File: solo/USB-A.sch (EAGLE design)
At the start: 27 parts, among them U1 USB_TRACES

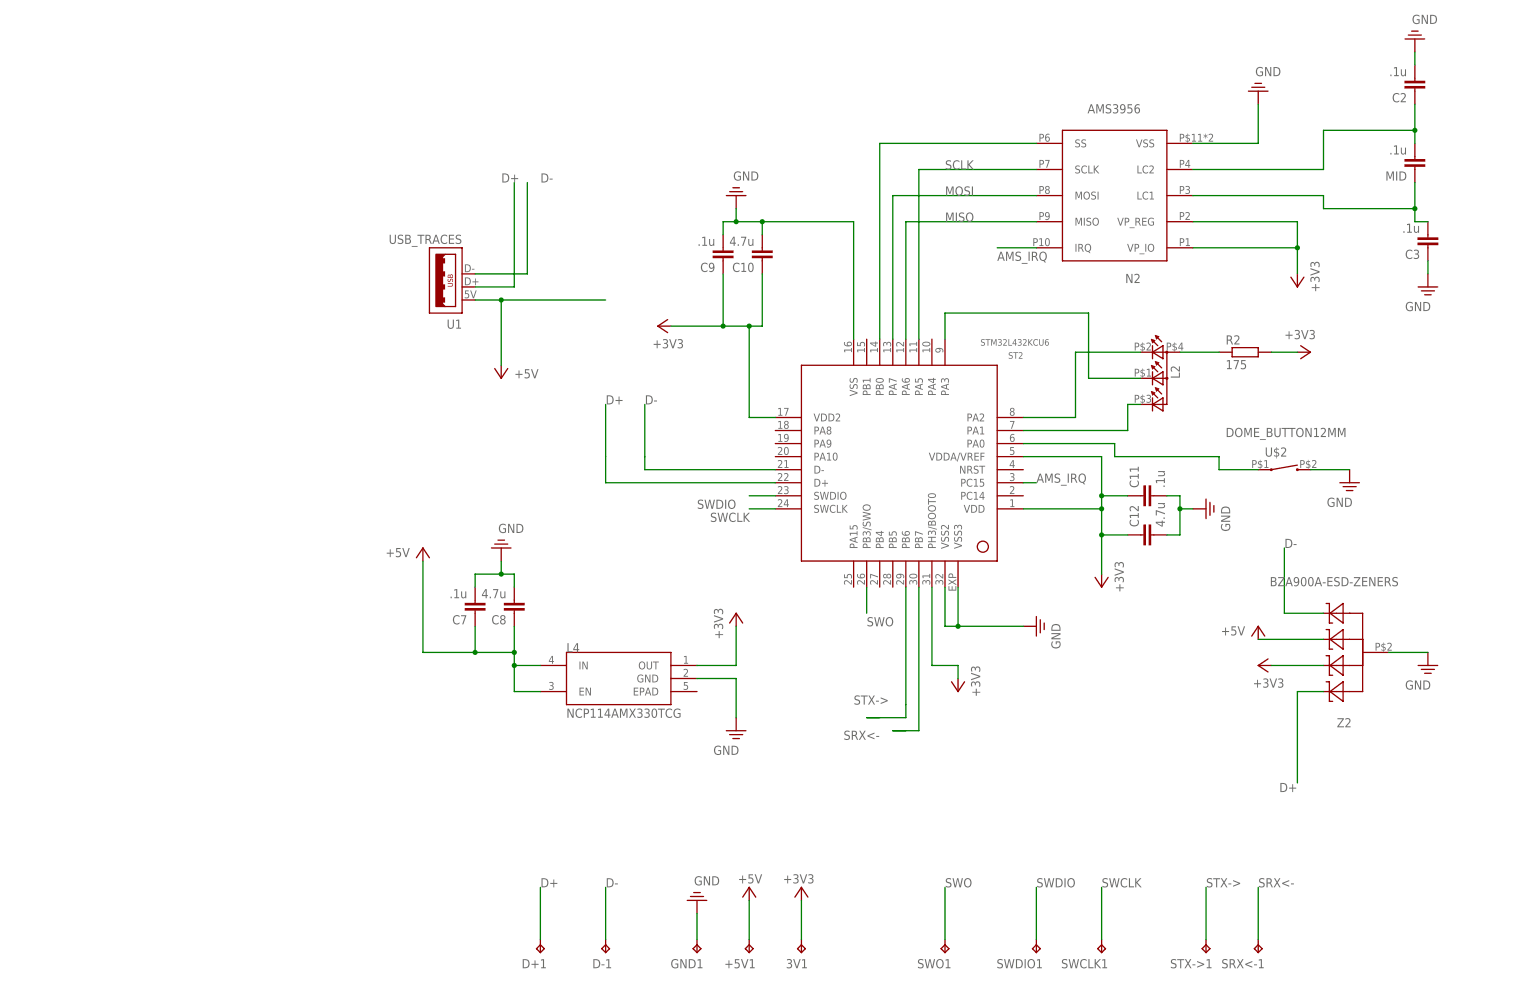
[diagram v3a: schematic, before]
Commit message: NFC designs
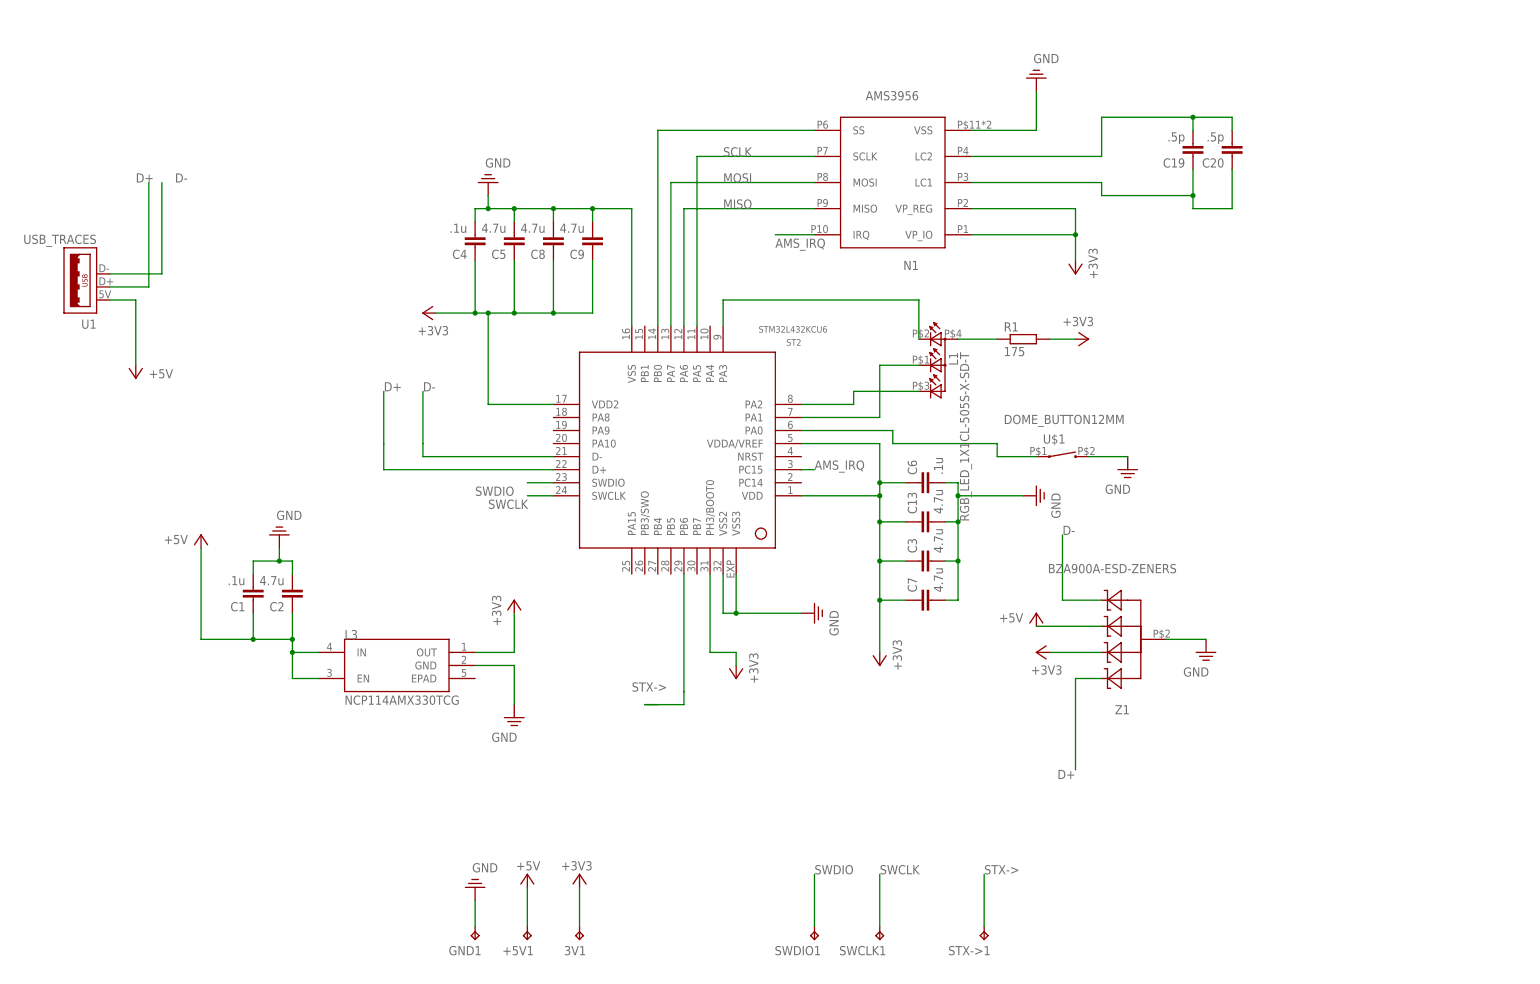
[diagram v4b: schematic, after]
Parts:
- removed C10, C12: 4.7u, efm-fido:CAPACITOR
- removed C11, MID: .1u, efm-fido:CAPACITOR
- removed D+1, D-1, SRX<-1, SWO1: TEST_POINT, efm-fido:TEST_POINT
- removed L2: EAST1616RGBA3-LED-RGBCL-505S-X-SD-T, efm-fido:EAST1616RGBA3-LED-RGBCL-505S-X-SD-T
- removed L4: NCP114AMX330TCG, efm-fido:NCP114AMX330TCG
- removed N2: AMS3956, efm-fido:AMS3956
- removed R2: 175, efm-fido:RESISTOR
- removed U$2: DOME_BUTTON12MM, efm-fido:DOME_BUTTON12MM
- removed Z2: BZA900A-ESD-ZENERS, efm-fido:BZA900A-ESD-ZENERS
- added C1, C4, C6: .1u, efm-fido:CAPACITOR
- added C13, C5: 4.7u, efm-fido:CAPACITOR
- added C19, C20: .5p, efm-fido:CAPACITOR
- added L1: RGB_LED_1X1CL-505S-X-SD-T, efm-fido:RGB_LED_1X1CL-505S-X-SD-T
- added L3: NCP114AMX330TCG, efm-fido:NCP114AMX330TCG
- added N1: AMS3956, efm-fido:AMS3956
- added R1: 175, efm-fido:RESISTOR
- added U$1: DOME_BUTTON12MM, efm-fido:DOME_BUTTON12MM
- added Z1: BZA900A-ESD-ZENERS, efm-fido:BZA900A-ESD-ZENERS
- C2, C3, C7, C9: value .1u -> 4.7u
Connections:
- removed net AMS_CS: N2.SS, ST2.PB0
- removed net N$18: L2.CGREEN, ST2.PA1
- removed net N$19: ST2.PA0, U$2.1
- removed net N$25: C2.1, MID.2, N2.LC2
- removed net N$26: C3.2, MID.1, N2.LC1
- removed net SRX<-: SRX<-1.TP, ST2.PB7
- removed net SWO: ST2.PB3/SWO, SWO1.TP
- new net AMS_CS2: N1.SS, ST2.PB0
- new net N$1: L1.A2, R1.1
- new net N$10: L1.CGREEN, ST2.PA2
- new net N$13: L1.CRED, ST2.PA3
- new net N$14: L1.CBLUE, ST2.PA1
- net +3V3: now also C13.1, C3.1, C4.1, C5.1, C6.1, C7.1, C8.1, L3.OUT, N1.VP_IO, N1.VP_REG, R1.2, Z1.C1; no longer C10.1, C11.1, C12.1, L4.OUT, N2.VP_IO, N2.VP_REG, R2.2, Z2.C1
- net +5V: now also C1.1, C2.1, L3.EN, L3.IN, Z1.C; no longer C7.1, C8.1, L4.EN, L4.IN, Z2.C
- net AMS_IRQ: now also N1.IRQ; no longer N2.IRQ
- net D+: now also Z1.C3; no longer D+1.TP, Z2.C3
- net D-: now also Z1.C2; no longer D-1.TP, Z2.C2
- net MISO: now also N1.MISO; no longer N2.MISO
- net MOSI: now also N1.MOSI; no longer N2.MOSI
- net N$15: now also ST2.PA0, U$1.1; no longer L2.A2, R2.1
- net N$16: now also C19.2, C20.2, N1.LC2; no longer L2.CRED, ST2.PA2
- net N$17: now also C19.1, C20.1, N1.LC1; no longer L2.CBLUE, ST2.PA3
- net PE: now also C1.2, C13.2, C3.2, C4.2, C5.2, C6.2, L3.GND, N1.VSS, U$1.2, Z1.P$1; no longer C10.2, C11.2, C12.2, C3.1, L4.GND, N2.VSS, U$2.2, Z2.P$1
- net SCLK: now also N1.SCLK; no longer N2.SCLK
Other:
- moved on the sheet: +5V1, 3V1, C2, C3, C7, C8, C9, GND1, ST2, STX->1, SWCLK1, SWDIO1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

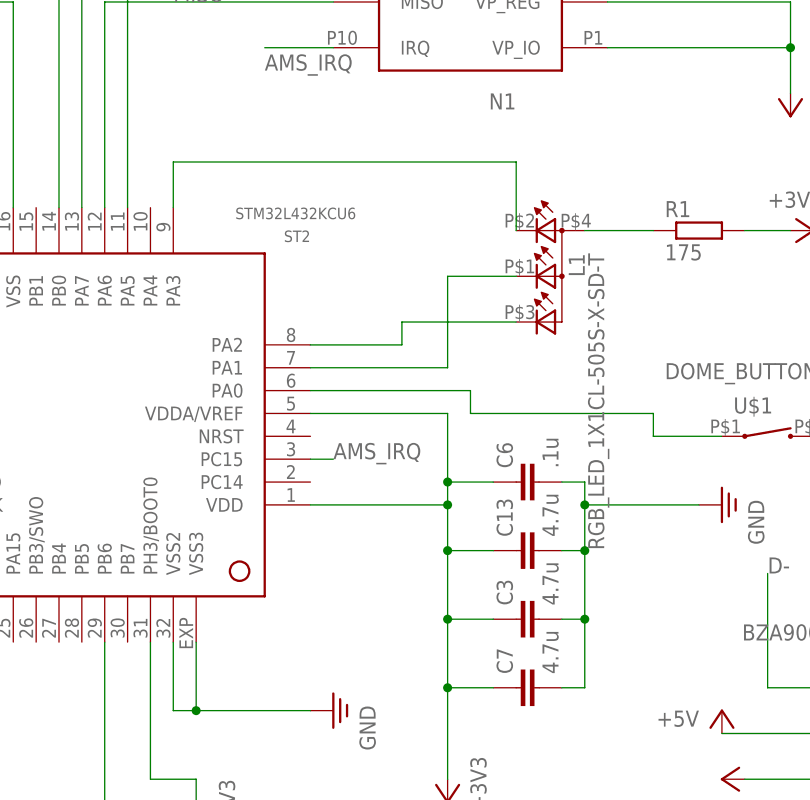
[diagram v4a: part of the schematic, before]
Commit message: go back to using old LED
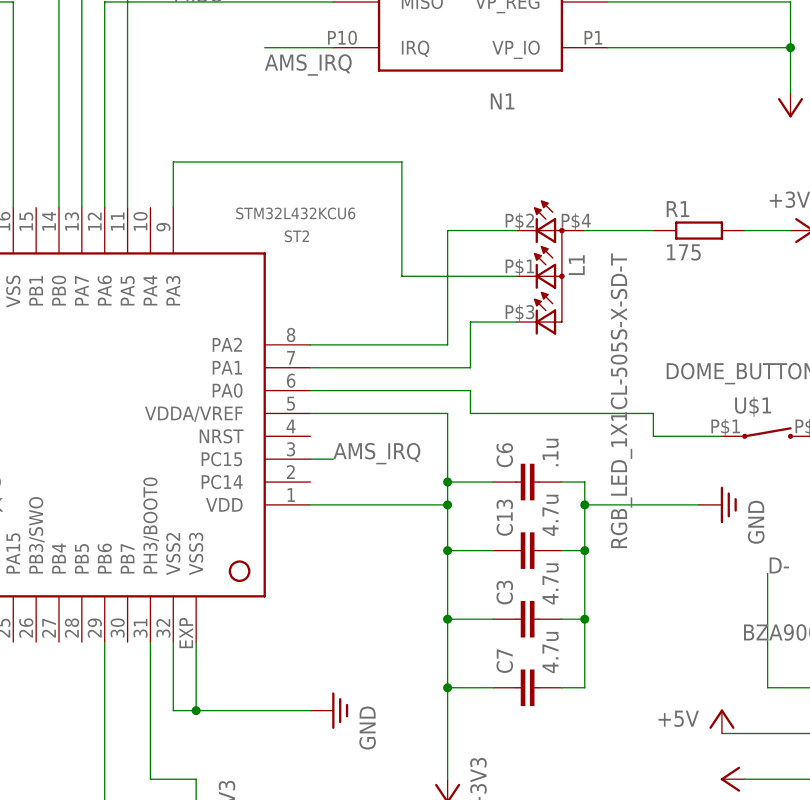
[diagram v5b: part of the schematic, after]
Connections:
- net N$10: now also L1.CRED; no longer L1.CGREEN
- net N$13: now also L1.CBLUE; no longer L1.CRED
- net N$14: now also L1.CGREEN; no longer L1.CBLUE
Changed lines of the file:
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@@
 <part name="C8" library="efm-fido" library_urn="urn:adsk.eagle:library:4245354" deviceset="CAPACITOR" device="" package3d_urn="urn:adsk.eagle:package:4245806/7" value="4.7u"/>
 <part name="C9" library="efm-fido" library_urn="urn:adsk.eagle:library:4245354" deviceset="CAPACITOR" device="" package3d_urn="urn:adsk.eagle:package:4245806/7" value="4.7u"/>
-<part name="L1" library="efm-fido" library_urn="urn:adsk.eagle:library:4245354" deviceset="RGB_LED_1X1" device="CL-505S-X-SD-T" package3d_urn="urn:adsk.eagle:package:4878740/7"/>
+<part name="L1" library="efm-fido" library_urn="urn:adsk.eagle:library:4245354" deviceset="RGB_LED_1X1" device="CL-505S-X-SD-T" package3d_urn="urn:adsk.eagle:package:4878740/8"/>
 </parts>
 <sheets>
@@
 <instance part="L1" gate="G$1" x="220.98" y="119.38" smashed="yes" rot="R270">
 <attribute name="NAME" x="224.282" y="121.92" size="1.778" layer="95" rot="R270"/>
-<attribute name="VALUE" x="226.441" y="121.92" size="1.778" layer="96" rot="R270"/>
+<attribute name="VALUE" x="228.981" y="121.92" size="1.778" layer="96" rot="R270"/>
 </instance>
 </instances>
@@
 <segment>
 <pinref part="ST2" gate="G$1" pin="PA2"/>
-<wire x1="205.74" y1="114.3" x2="205.74" y2="111.76" width="0.1524" layer="91"/>
-<wire x1="205.74" y1="111.76" x2="195.58" y2="111.76" width="0.1524" layer="91"/>
-<wire x1="218.44" y1="114.3" x2="205.74" y2="114.3" width="0.1524" layer="91"/>
-<pinref part="L1" gate="G$1" pin="CGREEN"/>
+<wire x1="210.82" y1="111.76" x2="195.58" y2="111.76" width="0.1524" layer="91"/>
+<wire x1="210.82" y1="111.76" x2="210.82" y2="124.46" width="0.1524" layer="91"/>
+<pinref part="L1" gate="G$1" pin="CRED"/>
+<wire x1="210.82" y1="124.46" x2="218.44" y2="124.46" width="0.1524" layer="91"/>
 </segment>
 </net>
 <net name="N$13" class="0">
 <segment>
-<wire x1="218.44" y1="132.08" x2="180.34" y2="132.08" width="0.1524" layer="91"/>
 <pinref part="ST2" gate="G$1" pin="PA3"/>
 <wire x1="180.34" y1="132.08" x2="180.34" y2="127" width="0.1524" layer="91"/>
-<pinref part="L1" gate="G$1" pin="CRED"/>
-<wire x1="218.44" y1="124.46" x2="218.44" y2="132.08" width="0.1524" layer="91"/>
+<wire x1="180.34" y1="132.08" x2="205.74" y2="132.08" width="0.1524" layer="91"/>
+<wire x1="205.74" y1="132.08" x2="205.74" y2="119.38" width="0.1524" layer="91"/>
+<pinref part="L1" gate="G$1" pin="CBLUE"/>
+<wire x1="205.74" y1="119.38" x2="218.44" y2="119.38" width="0.1524" layer="91"/>
 </segment>
 </net>
@@
 <segment>
 <pinref part="ST2" gate="G$1" pin="PA1"/>
-<wire x1="195.58" y1="109.22" x2="210.82" y2="109.22" width="0.1524" layer="91"/>
-<pinref part="L1" gate="G$1" pin="CBLUE"/>
-<wire x1="218.44" y1="119.38" x2="210.82" y2="119.38" width="0.1524" layer="91"/>
-<wire x1="210.82" y1="119.38" x2="210.82" y2="109.22" width="0.1524" layer="91"/>
-</segment>
-</net>
+<wire x1="195.58" y1="109.22" x2="213.36" y2="109.22" width="0.1524" layer="91"/>
+<wire x1="213.36" y1="109.22" x2="213.36" y2="114.3" width="0.1524" layer="91"/>
+<pinref part="L1" gate="G$1" pin="CGREEN"/>
+<wire x1="213.36" y1="114.3" x2="218.44" y2="114.3" width="0.1524" layer="91"/>
+</segment>
+</net>
